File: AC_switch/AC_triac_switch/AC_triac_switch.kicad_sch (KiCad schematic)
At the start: 1 part, among them Q1 BT137

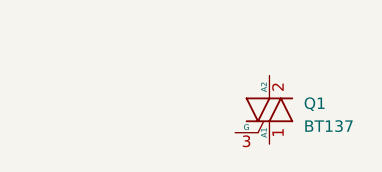
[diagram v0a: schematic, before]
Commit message: Added MOC3021M to schematic.
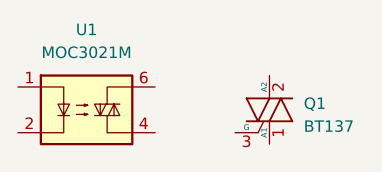
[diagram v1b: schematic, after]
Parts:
- added U1: MOC3021M, symbol Relay_SolidState:MOC3021M
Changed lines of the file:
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@@
 (kicad_sch (version 20230121) (generator eeschema)
   (paper "A4")
+  (symbol (lib_id "Relay_SolidState:MOC3021M") (at 118.11 110.49 0) (unit 1)
+    (in_bom yes) (on_board yes) (dnp no) (fields_autoplaced)
+    (property "Reference" "U1" (at 118.11 101.6 0)
+      (effects (font (size 1.27 1.27)))
+    )
+    (property "Value" "MOC3021M" (at 118.11 104.14 0)
+      (effects (font (size 1.27 1.27)))
+    )
+    (property "Footprint" "" (at 113.03 115.57 0)
+      (effects (font (size 1.27 1.27) italic) (justify left) hide)
+    )
+    (property "Datasheet" "https://www.onsemi.com/pub/Collateral/MOC3023M-D.PDF" (at 118.11 110.49 0)
+      (effects (font (size 1.27 1.27)) (justify left) hide)
+    )
+    (pin "1")
+    (pin "2")
+    (pin "5")
+    (pin "3")
+    (pin "6")
+    (pin "4")
+    (instances
+      (project "AC_triac_switch"
+        (path "/ddb0e52c-b99d-45b7-ae86-92b2e9148829"
+          (reference "U1") (unit 1)
+        )
+      )
+    )
+  )
   (symbol (lib_id "BT137:BT137") (at 138.43 110.49 0) (unit 1)
     (in_bom yes) (on_board yes) (dnp no) (fields_autoplaced)
